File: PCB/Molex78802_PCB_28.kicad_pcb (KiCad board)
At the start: 2 copper layers, 16.5 x 38 mm, 1 part

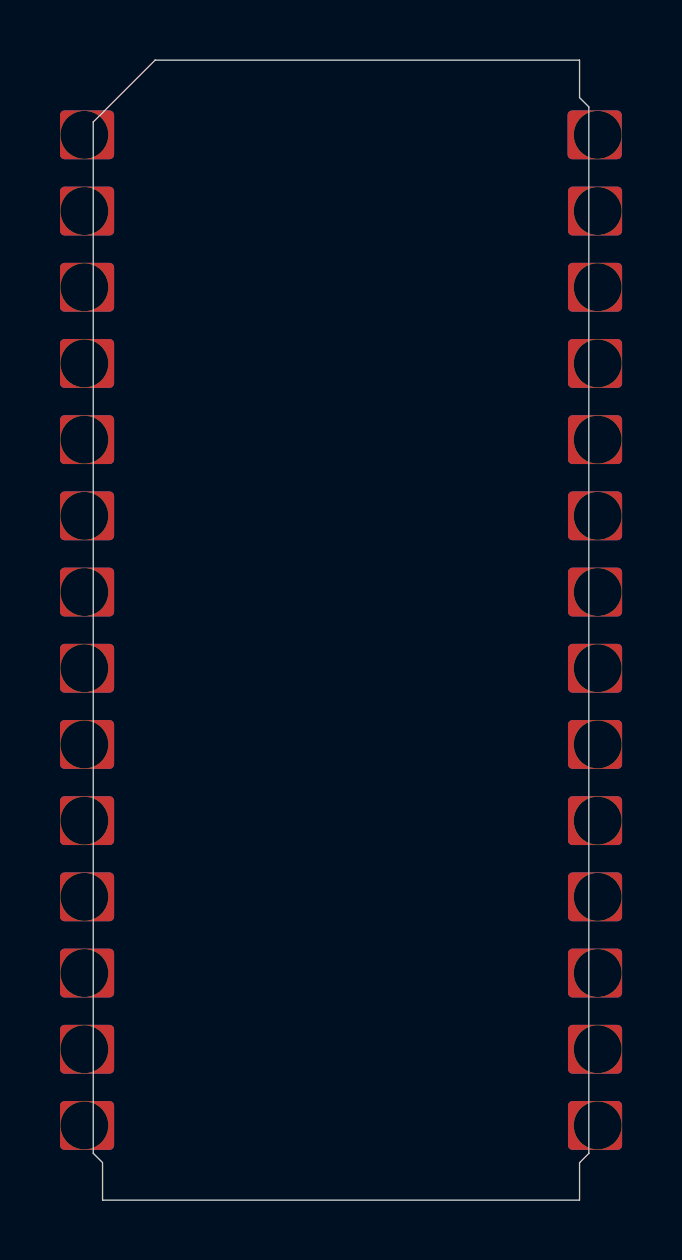
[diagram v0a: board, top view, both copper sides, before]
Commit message: improved fitment all around, simplified the pcb corners, removed junk from the scad model
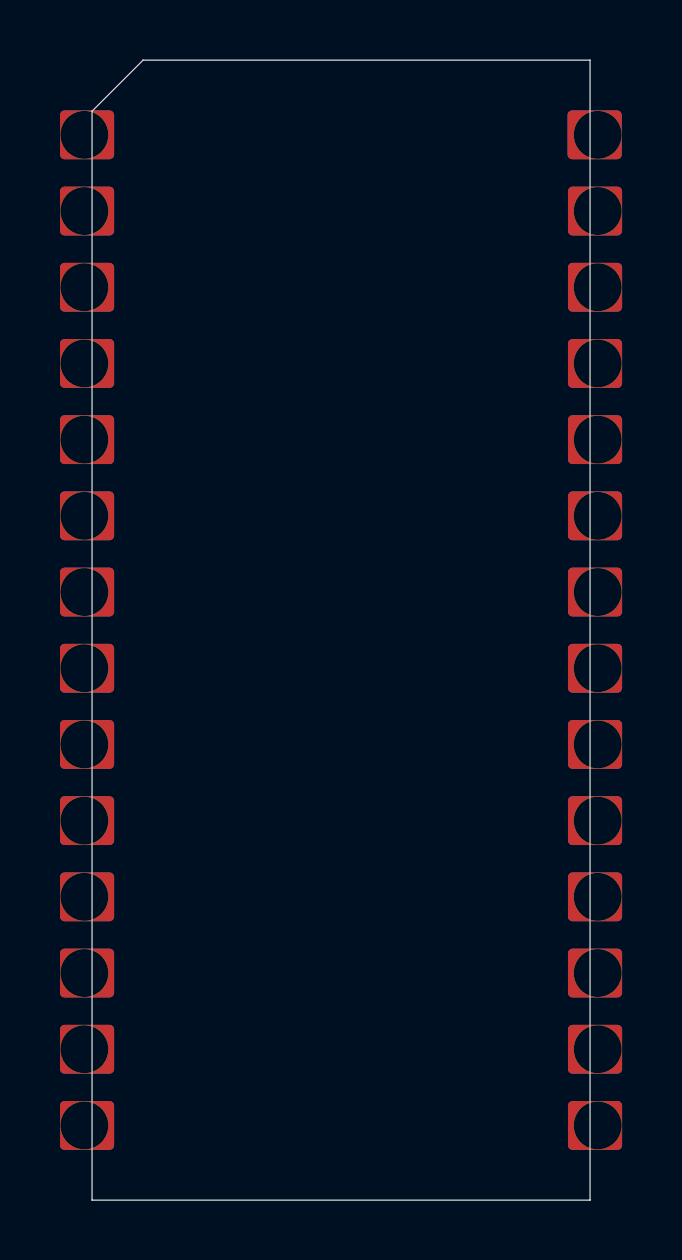
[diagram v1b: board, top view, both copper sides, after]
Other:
- board size 16.5 x 38 mm -> 16.6 x 38 mm
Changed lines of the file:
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@@
   (general
     (thickness 1.6)
-    (drawings 11)
+    (drawings 5)
     (tracks 0)
     (zones 0)
@@
     (title "Molex78802 PCB 28")
     (date 2021-05-20)
-    (rev 004)
+    (rev 005)
     (company b.kenyon.w@gmail.com)
   )
@@
     (fp_line (start -6 -17) (end -5.5 -17) (layer Dwgs.User) (width 0.01))
     (fp_line (start -6 -18.3) (end -6 -17) (layer Dwgs.User) (width 0.01))
-    (fp_line (start 7.2 -18.3) (end 7.2 18.3) (layer Dwgs.User) (width 0.01))
-    (fp_line (start -7.2 -18.3) (end -7.2 18.3) (layer Dwgs.User) (width 0.01))
-    (fp_line (start -7.2 -18.3) (end 7.2 -18.3) (layer Dwgs.User) (width 0.01))
-    (fp_line (start -7.2 18.3) (end 7.2 18.3) (layer Dwgs.User) (width 0.01))
-    (fp_line (start -8.255 0.0508) (end -8.255 -0.0508) (layer Dwgs.User) (width 0.002))
+    (fp_line (start 7.6 -18.3) (end 7.6 18.3) (layer Dwgs.User) (width 0.01))
+    (fp_line (start -7.6 -18.3) (end -7.6 18.3) (layer Dwgs.User) (width 0.01))
+    (fp_line (start -7.6 -18.3) (end 7.6 -18.3) (layer Dwgs.User) (width 0.01))
+    (fp_line (start -7.6 18.3) (end 7.6 18.3) (layer Dwgs.User) (width 0.01))
     (fp_poly (pts (xy 9.2156 1.9304) (xy 7.717 1.9304) (xy 7.717 0.6096) (xy 9.2156 0.6096)) (layer Top) (width 0.3048))
     (fp_poly (pts (xy 9.2156 -0.6096) (xy 7.717 -0.6096) (xy 7.717 -1.9304) (xy 9.2156 -1.9304)) (layer Top) (width 0.3048))
@@
     (fp_line (start -0.762 -21.59) (end 0.762 -21.59) (layer Eco1.User) (width 0.01))
     (fp_line (start -0.762 -19.05) (end -0.762 -21.59) (layer Eco1.User) (width 0.01))
-    (fp_line (start -7.95 19) (end 7.95 19) (layer Eco2.User) (width 0.01))
-    (fp_line (start 7.95 19) (end 7.95 17.75) (layer Eco2.User) (width 0.01))
-    (fp_line (start -7.95 19) (end -7.95 17.75) (layer Eco2.User) (width 0.01))
-    (fp_line (start 7.95 -17.75) (end 7.95 -19) (layer Eco2.User) (width 0.01))
-    (fp_line (start 8.26 17.44) (end 8.26 -17.44) (layer Eco2.User) (width 0.01))
-    (fp_line (start -8.26 17.44) (end -8.26 -16.94) (layer Eco2.User) (width 0.01))
-    (fp_line (start 7.95 -19) (end -6.2 -19) (layer Eco2.User) (width 0.01))
-    (fp_line (start -6.2 -19) (end -8.26 -16.94) (layer Eco2.User) (width 0.01))
+    (fp_line (start -8.3 19) (end 8.3 19) (layer Eco2.User) (width 0.01))
+    (fp_line (start 8.3 -19) (end -6.6 -19) (layer Eco2.User) (width 0.01))
     (fp_line (start 7.75716 17.78) (end 7.75716 12.7) (layer Dwgs.User) (width 0.01))
-    (fp_line (start 6.35 12.065) (end 6.35 15.24) (layer Dwgs.User) (width 0.05))
-    (fp_line (start 6.35 15.24) (end 7.747 15.24) (layer Dwgs.User) (width 0.05))
-    (fp_line (start 7.747 15.24) (end 7.467 15.52) (layer Dwgs.User) (width 0.05))
-    (fp_line (start 7.467 14.96) (end 7.747 15.24) (layer Dwgs.User) (width 0.05))
-    (fp_line (start 8.27 15.24) (end 8.55 15.52) (layer Dwgs.User) (width 0.05))
-    (fp_line (start 8.55 14.96) (end 8.27 15.24) (layer Dwgs.User) (width 0.05))
-    (fp_line (start 8.27 15.24) (end 9.667 15.24) (layer Dwgs.User) (width 0.05))
+    (fp_line (start 6.325 12.065) (end 6.325 15.24) (layer Dwgs.User) (width 0.05))
+    (fp_line (start 6.325 15.24) (end 7.722 15.24) (layer Dwgs.User) (width 0.05))
+    (fp_line (start 7.722 15.24) (end 7.442 15.52) (layer Dwgs.User) (width 0.05))
+    (fp_line (start 7.442 14.96) (end 7.722 15.24) (layer Dwgs.User) (width 0.05))
+    (fp_line (start 8.345 15.24) (end 8.625 15.52) (layer Dwgs.User) (width 0.05))
+    (fp_line (start 8.625 14.96) (end 8.345 15.24) (layer Dwgs.User) (width 0.05))
+    (fp_line (start 8.345 15.24) (end 9.742 15.24) (layer Dwgs.User) (width 0.05))
     (fp_line (start -5 -19) (end -5 -18) (layer Dwgs.User) (width 0.01))
     (fp_line (start -5 -18) (end 5 -18) (layer Dwgs.User) (width 0.01))
@@
     (fp_line (start -5 18) (end 5 18) (layer Dwgs.User) (width 0.01))
     (fp_line (start -5 19) (end 5 19) (layer Dwgs.User) (width 0.01))
-    (fp_line (start 7.95 17.75) (end 8.26 17.44) (layer Eco2.User) (width 0.01))
-    (fp_line (start 7.95 -17.75) (end 8.26 -17.44) (layer Eco2.User) (width 0.01))
-    (fp_line (start -7.95 17.75) (end -8.26 17.44) (layer Eco2.User) (width 0.01))
-    (fp_text user "0.7 border on bottom - 36.6 x 14.4 x 1.4 usable bottom" (at -5.5 -17) (layer Dwgs.User)
+    (fp_line (start -8.3 19) (end -8.3 -17.3) (layer Eco2.User) (width 0.01))
+    (fp_line (start 8.3 19) (end 8.3 -19) (layer Eco2.User) (width 0.01))
+    (fp_line (start -6.6 -19) (end -8.3 -17.3) (layer Eco2.User) (width 0.01))
+    (fp_text user "0.7 border on bottom - 36.4 x 15.0 x 1.4 usable bottom" (at -5.5 -17) (layer Dwgs.User)
       (effects (font (size 0.25 0.25) (thickness 0.02)) (justify left))
     )
@@
       (effects (font (size 1 1) (thickness 0.1)))
     )
-    (fp_text user "Board outline: 0.01mm grid, copy Eco2.User" (at -6 0 -90) (layer Eco2.User)
+    (fp_text user "Board outline: 0.1mm grid, copy Eco2.User" (at -6 0 -90) (layer Eco2.User)
       (effects (font (size 1 1) (thickness 0.1)))
     )
@@
     (pad 15 thru_hole circle (at 8.5552 16.51 180) (size 1.6002 1.6002) (drill 1.59766) (layers *.Cu *.Mask))
     (model ${KIPRJMOD}/000_LOCAL.pretty/3d/Molex78802_PCB_28.step
-      (offset (xyz 0 0 -0.18))
+      (offset (xyz 0 0 -0.16))
       (scale (xyz 1 1 1))
       (rotate (xyz 0 0 90))
     )
   )
-  (gr_line (start 139.2684 116.937) (end 138.9584 116.627) (layer Edge.Cuts) (width 0.01))
-  (gr_line (start 155.1684 81.437) (end 155.4784 81.747) (layer Edge.Cuts) (width 0.01))
-  (gr_line (start 155.1684 116.937) (end 155.4784 116.627) (layer Edge.Cuts) (width 0.01))
-  (gr_line (start 139.2684 116.937) (end 139.2684 118.187) (layer Edge.Cuts) (width 0.01))
-  (gr_line (start 138.9584 82.247) (end 138.9584 116.627) (layer Edge.Cuts) (width 0.01))
-  (gr_line (start 141.0184 80.187) (end 138.9584 82.247) (layer Edge.Cuts) (width 0.01))
-  (gr_line (start 155.1684 80.187) (end 141.0184 80.187) (layer Edge.Cuts) (width 0.01))
-  (gr_line (start 155.1684 81.437) (end 155.1684 80.187) (layer Edge.Cuts) (width 0.01))
-  (gr_line (start 155.4784 116.627) (end 155.4784 81.747) (layer Edge.Cuts) (width 0.01))
-  (gr_line (start 155.1684 118.187) (end 155.1684 116.937) (layer Edge.Cuts) (width 0.01))
-  (gr_line (start 139.2684 118.187) (end 155.1684 118.187) (layer Edge.Cuts) (width 0.01))
+  (gr_line (start 138.9184 81.887) (end 140.6184 80.187) (layer Edge.Cuts) (width 0.01))
+  (gr_line (start 138.9184 81.887) (end 138.9184 118.187) (layer Edge.Cuts) (width 0.01))
+  (gr_line (start 155.5184 80.187) (end 140.6184 80.187) (layer Edge.Cuts) (width 0.01))
+  (gr_line (start 155.5184 118.187) (end 155.5184 80.187) (layer Edge.Cuts) (width 0.01))
+  (gr_line (start 138.9184 118.187) (end 155.5184 118.187) (layer Edge.Cuts) (width 0.01))
 )
